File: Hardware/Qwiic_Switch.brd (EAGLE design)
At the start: 30.5 x 20.3 mm, 54 parts, among them J7 ISP, U4 ATTINY84-ARDUINO

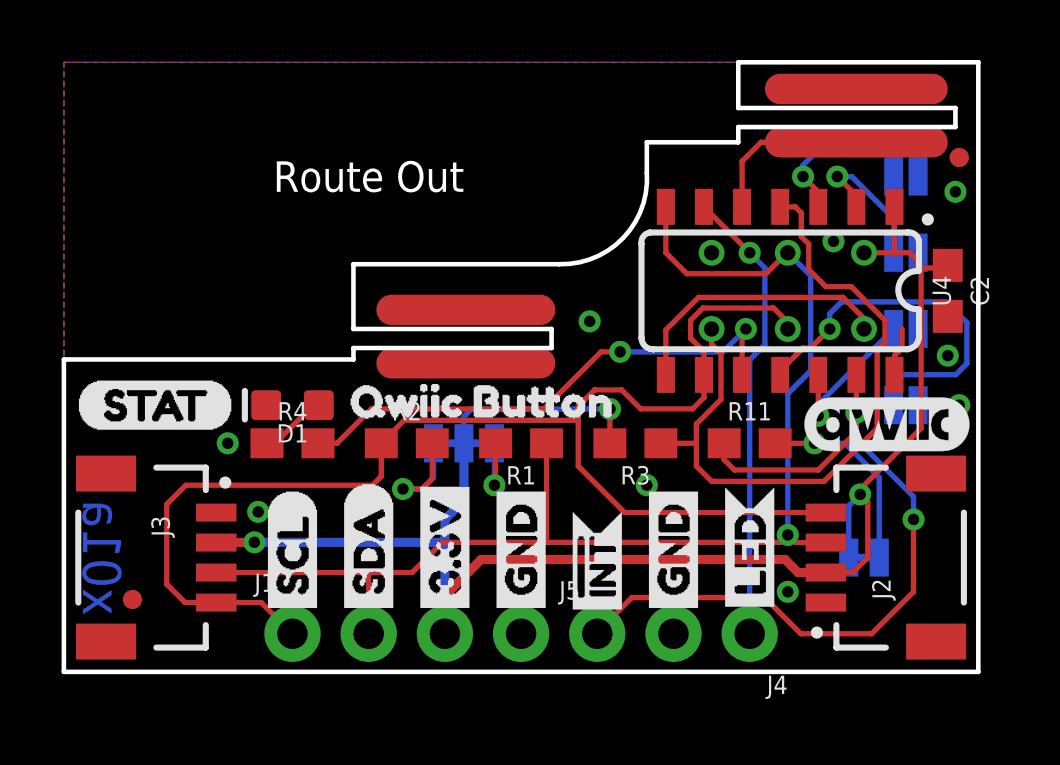
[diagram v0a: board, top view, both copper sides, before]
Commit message: Update schematic with I2C address
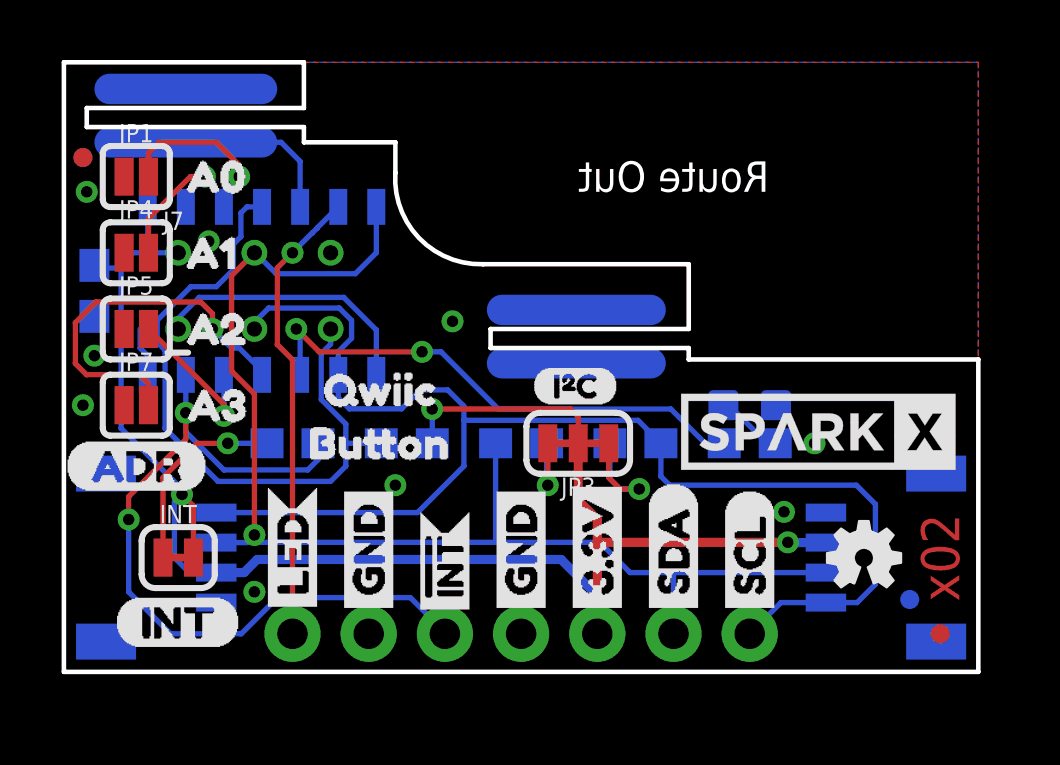
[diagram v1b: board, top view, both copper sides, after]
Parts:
- moved FRAME1 45.7 mm to (38.1, -21.6), flipped to the bottom
- moved U$9 30.5 mm to (0.00, 6.86), flipped to the top
- moved U$21 29.7 mm to (30.1, 8.89), flipped to the bottom
- moved JP2 29.2 mm to (0.64, 17.1), flipped to the top
- moved JP9 29.2 mm to (0.64, 17.1), flipped to the bottom
- moved C2 28.4 mm to (1.02, 12.7), flipped to the bottom
- moved U$4 27.2 mm to (1.65, 1.65), flipped to the top
- moved JP6 26.9 mm to (29.2, 1.27), flipped to the top
- moved JP8 25.9 mm to (28.2, 2.41), flipped to the bottom
- moved JP1 25.7 mm to (2.41, 16.5), flipped to the top
- moved JP4 25.7 mm to (2.41, 14.0), flipped to the top
- moved JP5 25.7 mm to (2.41, 11.4), flipped to the top
- moved JP7 25.7 mm to (2.41, 8.89), flipped to the top
- moved U$1 24.4 mm to (3.05, 8.26), flipped to the bottom
- moved U$28 24.4 mm to (3.05, 8.89), flipped to the top
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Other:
- outline, holes or cut-outs redrawn
- board text added: "x02"
- board text removed: "x01a"
